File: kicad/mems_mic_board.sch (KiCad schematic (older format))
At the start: 10 parts, among them J1 Conn_01x02_Male, J2 Conn_01x03_Male, J3 Conn_01x06_Male, J4 Conn_01x02_Male, J5 Conn_01x04_Male, J6 Conn_01x08_Male, J7 Conn_01x08_Male, U1 tactile_sw, U2 mems_mic, U3 mems_mic

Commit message: update
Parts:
- removed J1, J4: Conn_01x02_Male, mcu:Pin Header 2P, symbol Conn_01x02_Male
- removed J2: Conn_01x03_Male, mcu:Pin_Header_3P, symbol Conn_01x03_Male
- removed J5: Conn_01x04_Male, mcu:Pin Header 4P, symbol Conn_01x04_Male
- added J1: Conn_01x06_Male, mcu:Pin Header 6P, symbol Conn_01x06_Male
- added J2: Conn_01x01_Male, mcu:Pin_header_1P, symbol Conn_01x01_Male
- added J4: Conn_01x06_Female, mcu:Pin Header 6P, symbol Conn_01x06_Female
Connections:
- wire segments 40 -> 41
- no-connect marks 29 -> 33
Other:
- note added: "5V\n"
- note added: "Microchip RN4020\nBLE module"
- note added: "PC2 (DFSDM_CKOUT)"
- note added: "PC7 (DFSDM_DATAIN2)"
- note added: "RX"
- note added: "TX"
- note removed: "DFSDM_CKOUT"
- note removed: "E5V"
- note removed: "FTDI UART-USB converter"
- note removed: "PC7"
- note removed: "UART RX"
- note removed: "UART TX"
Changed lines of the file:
@@
 NoConn ~ 8050 2700
 Text Notes 8300 2650 0    60   ~ 0
-PC7
+PC7 (DFSDM_DATAIN2)
 $Comp
 L Conn_01x08_Male J7
@@
 Text Notes 2500 2650 0    60   ~ 0
 Vin
-$Comp
-L Conn_01x03_Male J2
-U 1 1 5BEA171D
-P 2400 2400
-F 0 "J2" H 2400 2600 50  0000 C CNN
-F 1 "Conn_01x03_Male" H 2400 2200 50  0000 C CNN
-F 2 "mcu:Pin_Header_3P" H 2400 2400 50  0001 C CNN
-F 3 "" H 2400 2400 50  0001 C CNN
-	1    2400 2400
-	1    0    0    -1
-$EndComp
-$Comp
-L Conn_01x02_Male J1
-U 1 1 5BEA174A
-P 2400 2000
-F 0 "J1" H 2400 2100 50  0000 C CNN
-F 1 "Conn_01x02_Male" H 2400 1800 50  0000 C CNN
-F 2 "mcu:Pin Header 2P" H 2400 2000 50  0001 C CNN
-F 3 "" H 2400 2000 50  0001 C CNN
-	1    2400 2000
-	1    0    0    -1
-$EndComp
 Text Notes 2150 2550 0    60   ~ 0
 Vin
@@
 Text Notes 2100 2050 0    60   ~ 0
 RESET
-NoConn ~ 2600 2400
 $Comp
 L tactile_sw U1
@@
 NoConn ~ 3350 1150
 NoConn ~ 4050 1150
-$Comp
-L Conn_01x04_Male J5
-U 1 1 5BEA287E
-P 5750 6450
-F 0 "J5" H 5750 6650 50  0000 C CNN
-F 1 "Conn_01x04_Male" H 5750 6150 50  0000 C CNN
-F 2 "mcu:Pin Header 4P" H 5750 6450 50  0001 C CNN
-F 3 "" H 5750 6450 50  0001 C CNN
-	1    5750 6450
-	0    1    -1   0
-$EndComp
-Text Notes 5900 6650 1    60   ~ 0
-5V
-Text Notes 5800 6700 1    60   ~ 0
+Text Notes 6100 6700 1    60   ~ 0
 GND
-Text Notes 5700 6850 1    60   ~ 0
-UART TX
-Text Notes 5600 6850 1    60   ~ 0
-UART RX
 Wire Wire Line
 	5900 3000 6600 3000
@@
 Wire Wire Line
 	5650 5850 5650 6250
-Wire Wire Line
-	8050 5750 5550 5750
-Wire Wire Line
-	5550 5750 5550 6250
-Wire Wire Line
-	5750 6250 5750 5500
-Wire Wire Line
-	5750 5500 4500 5500
-Connection ~ 4500 5500
 Wire Wire Line
 	2600 2000 3000 2000
@@
 Wire Wire Line
 	4300 950  4300 1700
-Text Notes 3950 7150 1    60   ~ 0
-DFSDM_CKOUT
+Text Notes 3950 7450 1    60   ~ 0
+PC2 (DFSDM_CKOUT)
+$Comp
+L Conn_01x06_Female J4
+U 1 1 5BEA871C
+P 5850 6450
+F 0 "J4" H 5850 6750 50  0000 C CNN
+F 1 "Conn_01x06_Female" H 5850 6050 50  0000 C CNN
+F 2 "mcu:Pin Header 6P" H 5850 6450 50  0001 C CNN
+F 3 "" H 5850 6450 50  0001 C CNN
+	1    5850 6450
+	0    1    1    0
+$EndComp
+Text Notes 5900 6650 1    60   ~ 0
+5V
+Text Notes 5800 6650 1    60   ~ 0
+RX
+Text Notes 5700 6650 1    60   ~ 0
+TX
+Wire Wire Line
+	6050 6250 6050 5400
+Wire Wire Line
+	6050 5400 4500 5400
+Connection ~ 4500 5400
+$Comp
+L Conn_01x06_Male J1
+U 1 1 5BEA8FE6
+P 2400 2200
+F 0 "J1" H 2400 2500 50  0000 C CNN
+F 1 "Conn_01x06_Male" H 2400 1800 50  0000 C CNN
+F 2 "mcu:Pin Header 6P" H 2400 2200 50  0001 C CNN
+F 3 "" H 2400 2200 50  0001 C CNN
+	1    2400 2200
+	1    0    0    -1
+$EndComp
+Text Notes 2200 2250 0    60   ~ 0
+5V\n
+Wire Wire Line
+	2600 2200 3000 2200
+Wire Wire Line
+	3000 2200 3000 5200
+Wire Wire Line
+	3000 5200 5850 5200
+Wire Wire Line
+	5850 5200 5850 6250
+Wire Wire Line
+	8050 5750 5750 5750
+Wire Wire Line
+	5750 5750 5750 6250
+NoConn ~ 2600 2400
 NoConn ~ 2600 2500
 $Comp
-L Conn_01x02_Male J4
-U 1 1 5BEA68EC
-P 3800 6450
-F 0 "J4" H 3800 6550 50  0000 C CNN
-F 1 "Conn_01x02_Male" H 3800 6250 50  0000 C CNN
-F 2 "mcu:Pin Header 2P" H 3800 6450 50  0001 C CNN
-F 3 "" H 3800 6450 50  0001 C CNN
-	1    3800 6450
+L Conn_01x01_Male J2
+U 1 1 5BEA9234
+P 3900 6450
+F 0 "J2" H 3900 6550 50  0000 C CNN
+F 1 "Conn_01x01_Male" H 3900 6350 50  0000 C CNN
+F 2 "mcu:Pin_header_1P" H 3900 6450 50  0001 C CNN
+F 3 "" H 3900 6450 50  0001 C CNN
+	1    3900 6450
 	0    -1   -1   0
 $EndComp
-Wire Wire Line
-	3800 6250 3800 5250
-Wire Wire Line
-	3800 5250 5850 5250
-Wire Wire Line
-	5850 5250 5850 6250
-Text Notes 3850 6700 1    60   ~ 0
-E5V
-Text Notes 5200 7050 0    60   ~ 0
-FTDI UART-USB converter
+Text Notes 5550 6950 0    60   ~ 0
+Microchip RN4020\nBLE module
+NoConn ~ 5550 6250
+NoConn ~ 5950 6250
+NoConn ~ -1000 1500
+NoConn ~ -950 1450
 $EndSCHEMATC

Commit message: update
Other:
- note added: "Mic L"
- note added: "Mic R"
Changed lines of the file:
@@
 NoConn ~ -1000 1500
 NoConn ~ -950 1450
+Text Notes 4950 3200 0    60   ~ 0
+Mic R
+Text Notes 4950 4100 0    60   ~ 0
+Mic L
 $EndSCHEMATC

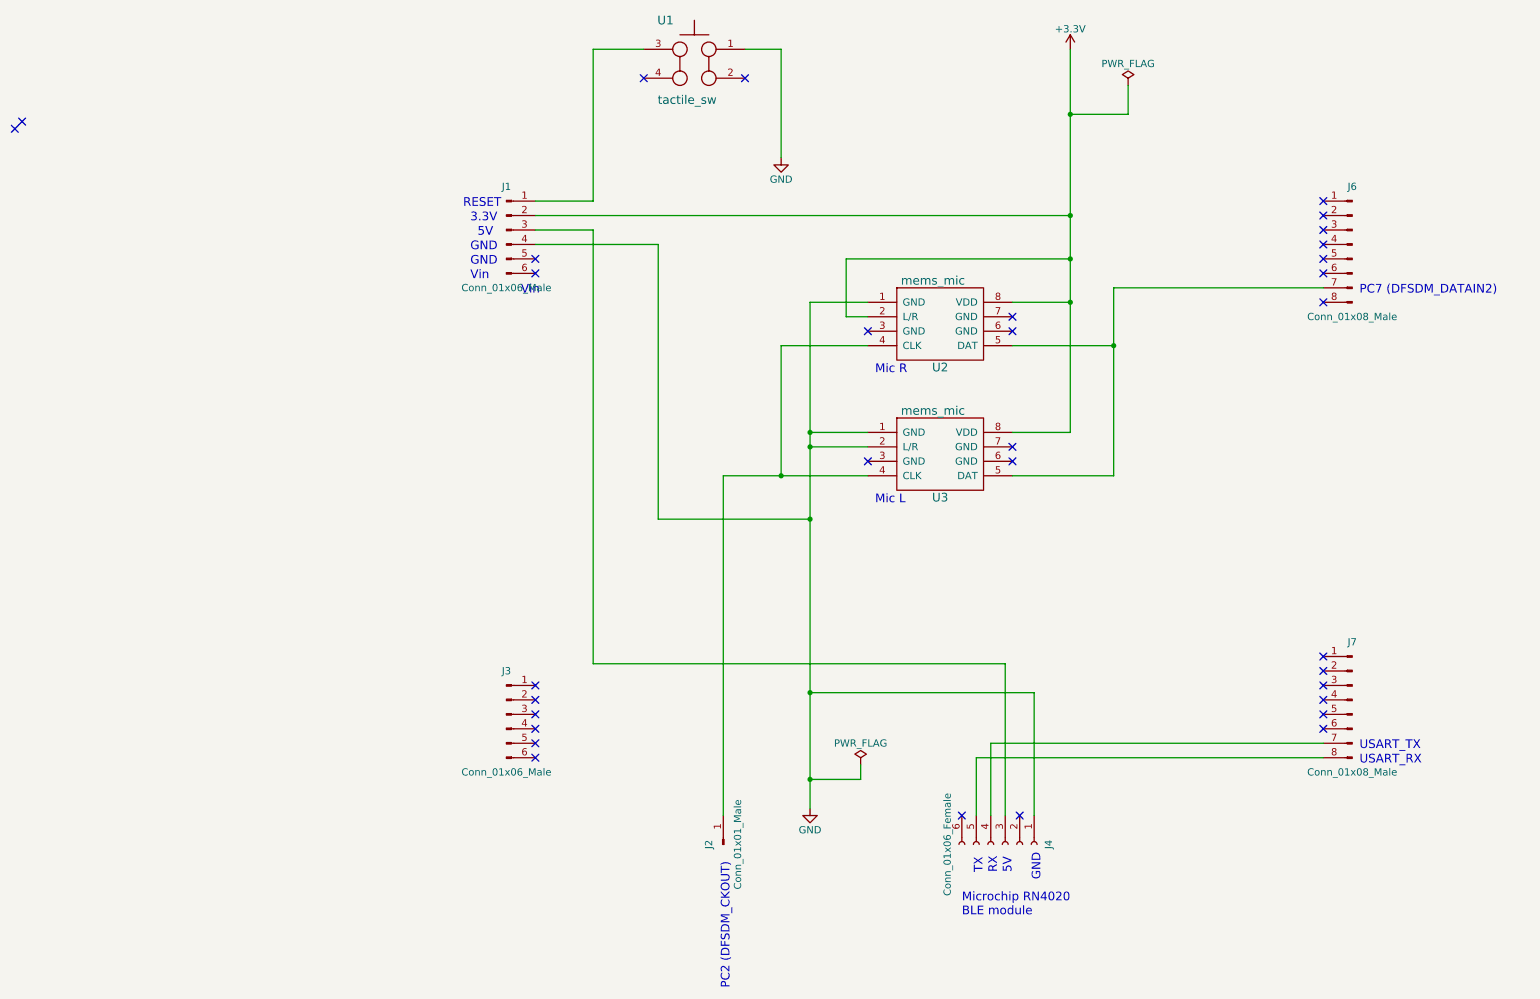
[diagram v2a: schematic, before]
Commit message: schematic update
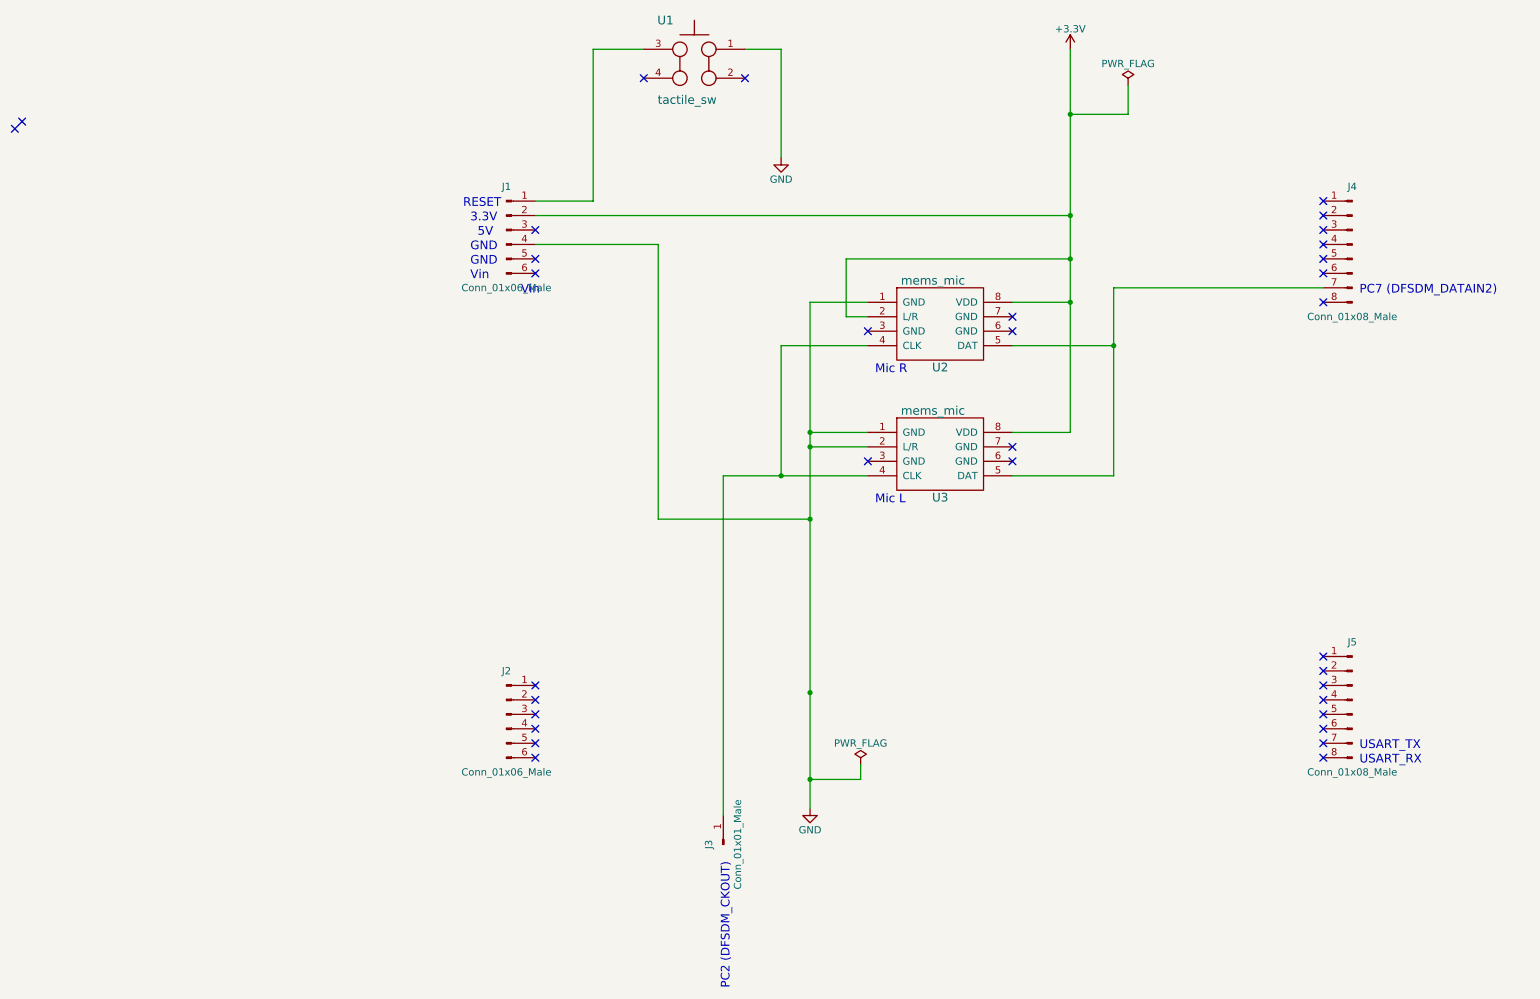
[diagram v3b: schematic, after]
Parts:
- removed J4: Conn_01x06_Female, mcu:Pin Header 6P, symbol Conn_01x06_Female
- renumbered J3 to J2, J2 to J3, J6 to J4, J7 to J5
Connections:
- no-connect marks 33 -> 34
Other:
- note removed: "5V"
- note removed: "Microchip RN4020\nBLE module"
- note removed: "RX"
- note removed: "TX"
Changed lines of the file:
@@
 Sheet 1 1
 Title "MEMS mic shield"
-Date "2018-11-13"
-Rev ""
+Date "2018-11-25"
+Rev "ver 0.2"
 Comp "https://github.com/araobp"
 Comment1 ""
@@
 $EndComp
 $Comp
-L Conn_01x08_Male J6
+L Conn_01x08_Male J4
 U 1 1 5BEA0A3B
 P 8250 2300
-F 0 "J6" H 8250 2700 50  0000 C CNN
+F 0 "J4" H 8250 2700 50  0000 C CNN
 F 1 "Conn_01x08_Male" H 8250 1800 50  0000 C CNN
 F 2 "mcu:Pin Header 8P" H 8250 2300 50  0001 C CNN
@@
 $EndComp
 $Comp
-L +3.3V #PWR01
+L +3.3V #PWR3
 U 1 1 5BEA0B18
 P 6300 950
-F 0 "#PWR01" H 6300 800 50  0001 C CNN
+F 0 "#PWR3" H 6300 800 50  0001 C CNN
 F 1 "+3.3V" H 6300 1090 50  0000 C CNN
 F 2 "" H 6300 950 50  0001 C CNN
@@
 NoConn ~ 4900 2900
 $Comp
-L GND #PWR02
+L GND #PWR2
 U 1 1 5BEA0B85
 P 4500 6200
-F 0 "#PWR02" H 4500 5950 50  0001 C CNN
+F 0 "#PWR2" H 4500 5950 50  0001 C CNN
 F 1 "GND" H 4500 6050 50  0000 C CNN
 F 2 "" H 4500 6200 50  0001 C CNN
@@
 PC7 (DFSDM_DATAIN2)
 $Comp
-L Conn_01x08_Male J7
+L Conn_01x08_Male J5
 U 1 1 5BEA0DD0
 P 8250 5450
-F 0 "J7" H 8250 5850 50  0000 C CNN
+F 0 "J5" H 8250 5850 50  0000 C CNN
 F 1 "Conn_01x08_Male" H 8250 4950 50  0000 C CNN
 F 2 "mcu:Pin Header 8P" H 8250 5450 50  0001 C CNN
@@
 NoConn ~ 8050 5650
 $Comp
-L Conn_01x06_Male J3
+L Conn_01x06_Male J2
 U 1 1 5BEA152F
 P 2400 5550
-F 0 "J3" H 2400 5850 50  0000 C CNN
+F 0 "J2" H 2400 5850 50  0000 C CNN
 F 1 "Conn_01x06_Male" H 2400 5150 50  0000 C CNN
 F 2 "mcu:Pin Header 6P" H 2400 5550 50  0001 C CNN
@@
 NoConn ~ 3350 1150
 NoConn ~ 4050 1150
-Text Notes 6100 6700 1    60   ~ 0
-GND
 Wire Wire Line
 	5900 3000 6600 3000
@@
 Connection ~ 6300 2400
 Wire Wire Line
-	8050 5850 5650 5850
-Wire Wire Line
-	5650 5850 5650 6250
-Wire Wire Line
 	2600 2000 3000 2000
 Wire Wire Line
@@
 	3000 950  3350 950
 $Comp
-L GND #PWR03
+L GND #PWR1
 U 1 1 5BEA39CA
 P 4300 1700
-F 0 "#PWR03" H 4300 1450 50  0001 C CNN
+F 0 "#PWR1" H 4300 1450 50  0001 C CNN
 F 1 "GND" H 4300 1550 50  0000 C CNN
 F 2 "" H 4300 1700 50  0001 C CNN
@@
 Connection ~ 6600 3000
 $Comp
-L PWR_FLAG #FLG04
+L PWR_FLAG #FLG2
 U 1 1 5BEA4D7E
 P 6700 1200
-F 0 "#FLG04" H 6700 1275 50  0001 C CNN
+F 0 "#FLG2" H 6700 1275 50  0001 C CNN
 F 1 "PWR_FLAG" H 6700 1350 50  0000 C CNN
 F 2 "" H 6700 1200 50  0001 C CNN
@@
 $EndComp
 $Comp
-L PWR_FLAG #FLG05
+L PWR_FLAG #FLG1
 U 1 1 5BEA4DA6
 P 4850 5900
-F 0 "#FLG05" H 4850 5975 50  0001 C CNN
+F 0 "#FLG1" H 4850 5975 50  0001 C CNN
 F 1 "PWR_FLAG" H 4850 6050 50  0000 C CNN
 F 2 "" H 4850 5900 50  0001 C CNN
@@
 Text Notes 3950 7450 1    60   ~ 0
 PC2 (DFSDM_CKOUT)
-$Comp
-L Conn_01x06_Female J4
-U 1 1 5BEA871C
-P 5850 6450
-F 0 "J4" H 5850 6750 50  0000 C CNN
-F 1 "Conn_01x06_Female" H 5850 6050 50  0000 C CNN
-F 2 "mcu:Pin Header 6P" H 5850 6450 50  0001 C CNN
-F 3 "" H 5850 6450 50  0001 C CNN
-	1    5850 6450
-	0    1    1    0
-$EndComp
-Text Notes 5900 6650 1    60   ~ 0
-5V
-Text Notes 5800 6650 1    60   ~ 0
-RX
-Text Notes 5700 6650 1    60   ~ 0
-TX
-Wire Wire Line
-	6050 6250 6050 5400
-Wire Wire Line
-	6050 5400 4500 5400
 Connection ~ 4500 5400
 $Comp
@@
 Text Notes 2200 2250 0    60   ~ 0
 5V\n
-Wire Wire Line
-	2600 2200 3000 2200
-Wire Wire Line
-	3000 2200 3000 5200
-Wire Wire Line
-	3000 5200 5850 5200
-Wire Wire Line
-	5850 5200 5850 6250
-Wire Wire Line
-	8050 5750 5750 5750
-Wire Wire Line
-	5750 5750 5750 6250
 NoConn ~ 2600 2400
 NoConn ~ 2600 2500
 $Comp
-L Conn_01x01_Male J2
+L Conn_01x01_Male J3
 U 1 1 5BEA9234
 P 3900 6450
-F 0 "J2" H 3900 6550 50  0000 C CNN
+F 0 "J3" H 3900 6550 50  0000 C CNN
 F 1 "Conn_01x01_Male" H 3900 6350 50  0000 C CNN
 F 2 "mcu:Pin_header_1P" H 3900 6450 50  0001 C CNN
@@
 	0    -1   -1   0
 $EndComp
-Text Notes 5550 6950 0    60   ~ 0
-Microchip RN4020\nBLE module
-NoConn ~ 5550 6250
-NoConn ~ 5950 6250
 NoConn ~ -1000 1500
 NoConn ~ -950 1450
@@
 Text Notes 4950 4100 0    60   ~ 0
 Mic L
+NoConn ~ 8050 5750
+NoConn ~ 8050 5850
+NoConn ~ 2600 2200
 $EndSCHEMATC

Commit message: update pattern
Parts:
- removed J1: Conn_01x06_Male, mcu:Pin Header 6P, symbol Conn_01x06_Male
- removed J4: Conn_01x08_Male, mcu:Pin Header 8P, symbol Conn_01x08_Male
- added J1: Conn_01x08_Male, mcu:Pin Header 8P, symbol Conn_01x08_Male
- added J4: Conn_01x10_Male, mcu:Pin Header 10P, symbol Conn_01x10_Male
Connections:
- net +3V3: now also J1.4 (Pin_4)
- net GND: now also U1.2, J1.6 (Pin_6); no longer U1.1
- net at U2.5 (DAT), U3.5 (DAT): now also J4.9 (Pin_9)
- net at U1.4: now also J1.3 (Pin_3)
- no-connect marks 34 -> 38
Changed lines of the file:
@@
 $EndComp
 $Comp
-L Conn_01x08_Male J4
-U 1 1 5BEA0A3B
-P 8250 2300
-F 0 "J4" H 8250 2700 50  0000 C CNN
-F 1 "Conn_01x08_Male" H 8250 1800 50  0000 C CNN
-F 2 "mcu:Pin Header 8P" H 8250 2300 50  0001 C CNN
-F 3 "" H 8250 2300 50  0001 C CNN
-	1    8250 2300
-	-1   0    0    -1
-$EndComp
-$Comp
-L +3.3V #PWR3
+L +3.3V #PWR01
 U 1 1 5BEA0B18
 P 6300 950
-F 0 "#PWR3" H 6300 800 50  0001 C CNN
+F 0 "#PWR01" H 6300 800 50  0001 C CNN
 F 1 "+3.3V" H 6300 1090 50  0000 C CNN
 F 2 "" H 6300 950 50  0001 C CNN
@@
 NoConn ~ 4900 2900
 $Comp
-L GND #PWR2
+L GND #PWR02
 U 1 1 5BEA0B85
 P 4500 6200
-F 0 "#PWR2" H 4500 5950 50  0001 C CNN
+F 0 "#PWR02" H 4500 5950 50  0001 C CNN
 F 1 "GND" H 4500 6050 50  0000 C CNN
 F 2 "" H 4500 6200 50  0001 C CNN
@@
 	0    1    1    0
 $EndComp
-NoConn ~ 3350 1150
-NoConn ~ 4050 1150
 Wire Wire Line
 	5900 3000 6600 3000
@@
 	2600 2000 3000 2000
 Wire Wire Line
-	3000 2000 3000 950
-Wire Wire Line
-	3000 950  3350 950
-$Comp
-L GND #PWR1
+	3000 2000 3000 1150
+Wire Wire Line
+	3000 1150 3350 1150
+$Comp
+L GND #PWR03
 U 1 1 5BEA39CA
 P 4300 1700
-F 0 "#PWR1" H 4300 1450 50  0001 C CNN
+F 0 "#PWR03" H 4300 1450 50  0001 C CNN
 F 1 "GND" H 4300 1550 50  0000 C CNN
 F 2 "" H 4300 1700 50  0001 C CNN
@@
 $EndComp
 Wire Wire Line
-	4050 950  4300 950
+	4050 1150 4300 1150
 Wire Wire Line
 	2600 2300 3450 2300
@@
 Connection ~ 6600 3000
 $Comp
-L PWR_FLAG #FLG2
+L PWR_FLAG #FLG04
 U 1 1 5BEA4D7E
 P 6700 1200
-F 0 "#FLG2" H 6700 1275 50  0001 C CNN
+F 0 "#FLG04" H 6700 1275 50  0001 C CNN
 F 1 "PWR_FLAG" H 6700 1350 50  0000 C CNN
 F 2 "" H 6700 1200 50  0001 C CNN
@@
 $EndComp
 $Comp
-L PWR_FLAG #FLG1
+L PWR_FLAG #FLG05
 U 1 1 5BEA4DA6
 P 4850 5900
-F 0 "#FLG1" H 4850 5975 50  0001 C CNN
+F 0 "#FLG05" H 4850 5975 50  0001 C CNN
 F 1 "PWR_FLAG" H 4850 6050 50  0000 C CNN
 F 2 "" H 4850 5900 50  0001 C CNN
@@
 Connection ~ 4500 6000
 Wire Wire Line
-	4300 950  4300 1700
+	4300 1150 4300 1700
 Text Notes 3950 7450 1    60   ~ 0
 PC2 (DFSDM_CKOUT)
 Connection ~ 4500 5400
-$Comp
-L Conn_01x06_Male J1
-U 1 1 5BEA8FE6
-P 2400 2200
-F 0 "J1" H 2400 2500 50  0000 C CNN
-F 1 "Conn_01x06_Male" H 2400 1800 50  0000 C CNN
-F 2 "mcu:Pin Header 6P" H 2400 2200 50  0001 C CNN
-F 3 "" H 2400 2200 50  0001 C CNN
-	1    2400 2200
-	1    0    0    -1
-$EndComp
 Text Notes 2200 2250 0    60   ~ 0
 5V\n
@@
 NoConn ~ 8050 5850
 NoConn ~ 2600 2200
+$Comp
+L Conn_01x08_Male J1
+U 1 1 5C5A0EE3
+P 2400 2100
+F 0 "J1" H 2400 2500 50  0000 C CNN
+F 1 "Conn_01x08_Male" H 2400 1600 50  0000 C CNN
+F 2 "mcu:Pin Header 8P" H 2400 2100 50  0001 C CNN
+F 3 "" H 2400 2100 50  0001 C CNN
+	1    2400 2100
+	1    0    0    -1
+$EndComp
+NoConn ~ 2600 1800
+NoConn ~ 2600 1900
+$Comp
+L Conn_01x10_Male J4
+U 1 1 5C5A0FF3
+P 8250 2200
+F 0 "J4" H 8250 2700 50  0000 C CNN
+F 1 "Conn_01x10_Male" H 8250 1600 50  0000 C CNN
+F 2 "mcu:Pin Header 10P" H 8250 2200 50  0001 C CNN
+F 3 "" H 8250 2200 50  0001 C CNN
+	1    8250 2200
+	-1   0    0    -1
+$EndComp
+NoConn ~ 8050 1900
+NoConn ~ 8050 1800
+NoConn ~ 3350 950
+NoConn ~ 4050 950
 $EndSCHEMATC

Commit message: update
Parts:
- added J6: Conn_01x04_Female, mcu:pin-socket-4p, symbol Conn_01x04_Female
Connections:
- net GND: now also J6.4 (Pin_4)
- net 5V: now reaches J1.5 (Pin_5)
- net 5V: now also J6.1 (Pin_1)
- net SCL: now reaches J4.1 (Pin_1)
- net SCL: now also J6.2 (Pin_2)
- net SDA: now reaches J4.2 (Pin_2)
- net SDA: now also J6.3 (Pin_3)
- no-connect marks 38 -> 35
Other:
- note added: "LCD"
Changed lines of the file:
@@
 NoConn ~ 8050 5750
 NoConn ~ 8050 5850
-NoConn ~ 2600 2200
 $Comp
 L Conn_01x08_Male J1
@@
 	-1   0    0    -1
 $EndComp
-NoConn ~ 8050 1900
-NoConn ~ 8050 1800
 NoConn ~ 3350 950
 NoConn ~ 4050 950
+$Comp
+L Conn_01x04_Female J6
+U 1 1 5C792525
+P 6950 6050
+F 0 "J6" H 6950 6250 50  0000 C CNN
+F 1 "Conn_01x04_Female" H 6950 5750 50  0000 C CNN
+F 2 "mcu:pin-socket-4p" H 6950 6050 50  0001 C CNN
+F 3 "" H 6950 6050 50  0001 C CNN
+	1    6950 6050
+	0    -1   1    0
+$EndComp
+Wire Wire Line
+	8050 1800 6950 1800
+Wire Wire Line
+	6950 1800 6950 5850
+Wire Wire Line
+	8050 1900 7050 1900
+Wire Wire Line
+	7050 1900 7050 5850
+Wire Wire Line
+	2600 2200 3350 2200
+Wire Wire Line
+	3350 2200 3350 4750
+Wire Wire Line
+	3350 4750 6850 4750
+Wire Wire Line
+	6850 4750 6850 5850
+$Comp
+L GND #PWR06
+U 1 1 5C79271E
+P 7600 6100
+F 0 "#PWR06" H 7600 5850 50  0001 C CNN
+F 1 "GND" H 7600 5950 50  0000 C CNN
+F 2 "" H 7600 6100 50  0001 C CNN
+F 3 "" H 7600 6100 50  0001 C CNN
+	1    7600 6100
+	1    0    0    -1
+$EndComp
+Wire Wire Line
+	7150 5850 7150 4750
+Wire Wire Line
+	7150 4750 7600 4750
+Wire Wire Line
+	7600 4750 7600 6100
+Text Label 7400 1800 0    60   ~ 0
+SCL
+Text Label 7400 1900 0    60   ~ 0
+SDA
+Text Label 6700 4750 0    60   ~ 0
+5V
+Text Label 7200 4750 0    60   ~ 0
+GND
+Text Notes 6900 6200 0    60   ~ 0
+LCD
 $EndSCHEMATC
